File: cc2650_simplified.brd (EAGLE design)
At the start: 50.5 x 22.9 mm, 13 parts, among them IC4 CC2650MODAMOHR, U402 TPS62233DRY

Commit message: Changed Voltage Regulator to 3.3V output.
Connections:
- removed net NRESET: IC4.13, JP2.16, JTAG_CONNECTOR.10
- removed net VBAT: JP3.3
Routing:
- net NRESET: track 41.6 -> 0.00 mm
- net VBAT: track 19.8 -> 0.00 mm
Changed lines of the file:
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@@
 <wire x1="13.08" y1="1.4" x2="15.62" y2="1.4" width="0" layer="19" extent="1-1"/>
-</signal>
-<signal name="NRESET">
-<contactref element="JTAG_CONNECTOR" pad="10"/>
-<contactref element="IC4" pad="13"/>
-<contactref element="JP2" pad="16"/>
-<wire x1="33.5" y1="9.5" x2="34" y2="9.5" width="0.2032" layer="1"/>
-<wire x1="30" y1="6" x2="33.5" y2="9.5" width="0.2032" layer="1"/>
-<wire x1="30" y1="5" x2="30" y2="6" width="0.2032" layer="1"/>
-<wire x1="34" y1="9.5" x2="33.83" y2="9.6" width="0.2032" layer="1"/>
-<wire x1="26.5" y1="3" x2="27.5" y2="4" width="0.2032" layer="1"/>
-<wire x1="27.5" y1="4" x2="27.682" y2="4.27" width="0.2032" layer="1"/>
-<wire x1="5.46" y1="1.4" x2="5.46" y2="1.46" width="0.2" layer="16"/>
-<wire x1="5.46" y1="1.46" x2="7" y2="3" width="0.2" layer="16"/>
-<wire x1="5.46" y1="1.4" x2="5.46" y2="1.46" width="0.2" layer="1"/>
-<wire x1="5.46" y1="1.46" x2="7" y2="3" width="0.2" layer="1"/>
-<wire x1="9" y1="3" x2="7" y2="3" width="0.2" layer="1"/>
-<wire x1="9" y1="3" x2="13.75" y2="3" width="0.2" layer="1"/>
-<wire x1="13.75" y1="3" x2="26.5" y2="3" width="0.2" layer="1"/>
-<wire x1="11.25" y1="5.25" x2="9" y2="3" width="0.2" layer="1"/>
-<wire x1="14.875" y1="4.125" x2="13.75" y2="3" width="0.2" layer="1"/>
-<wire x1="27.682" y1="4.27" x2="29.27" y2="4.27" width="0.2" layer="1"/>
-<wire x1="29.27" y1="4.27" x2="30" y2="5" width="0.2" layer="1"/>
-<wire x1="14.875" y1="4.125" x2="14.875" y2="5.995" width="0.2" layer="1"/>
-<wire x1="14.875" y1="5.995" x2="14.88" y2="6" width="0.2" layer="1"/>
 </signal>
 <signal name="JTAG_TMS">
@@
 <contactref element="IC4" pad="22"/>
 <contactref element="IC4" pad="23"/>
-<contactref element="JTAG_CONNECTOR" pad="1"/>
 <contactref element="JP3" pad="4"/>
 <contactref element="JP3" pad="6"/>
@@
 <wire x1="22.5" y1="9" x2="23.5" y2="9" width="0.2032" layer="1"/>
 <wire x1="22.5" y1="9" x2="22" y2="9" width="0.2032" layer="1"/>
-<wire x1="23.5" y1="9" x2="23.618" y2="9.35" width="0.2032" layer="1"/>
 <wire x1="41.5" y1="4.5" x2="41" y2="4.5" width="0.2032" layer="1"/>
 <wire x1="41" y1="4.5" x2="40.68" y2="4.55" width="0.2032" layer="1"/>
@@
 <wire x1="12.87825625" y1="2.9906" x2="14.9906" y2="2.9906" width="0.2" layer="16"/>
 <via x="17" y="4.5" extent="1-16" drill="0.35"/>
+<contactref element="JTAG_CONNECTOR" pad="1"/>
+<wire x1="23.5" y1="9" x2="23.618" y2="9.35" width="0" layer="19" extent="1-1"/>
 <wire x1="17.75" y1="5.25" x2="20.35" y2="7.35" width="0" layer="19" extent="1-1"/>
 </signal>
-<signal name="VBAT">
-<contactref element="JP3" pad="3"/>
-<wire x1="20.5" y1="21.5" x2="15.5" y2="16.5" width="0.2032" layer="16"/>
-<wire x1="20.5" y1="21.5" x2="20.79" y2="21.68" width="0.2032" layer="16"/>
-<wire x1="15.5" y1="16.5" x2="3.146" y2="16.5" width="0.2" layer="16"/>
-</signal>
 <signal name="EN">

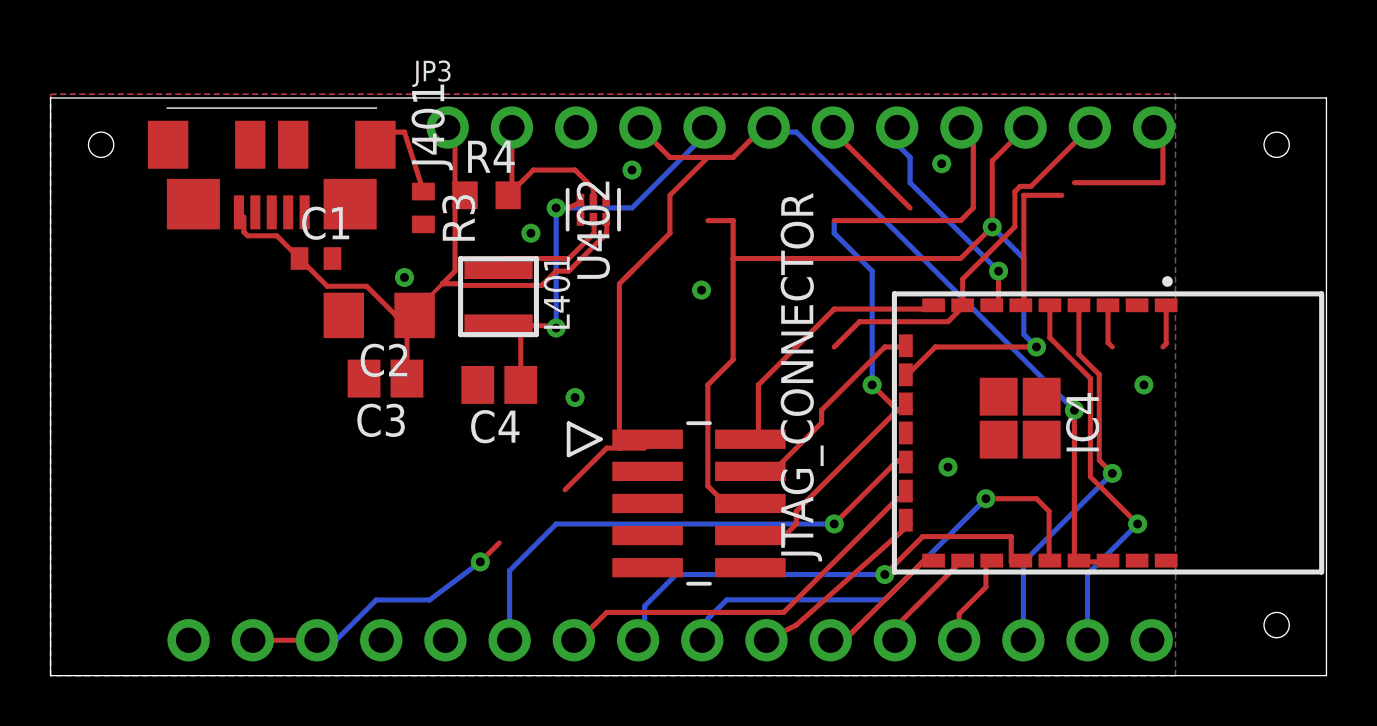
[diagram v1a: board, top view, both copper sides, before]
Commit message: fixed broken connection and missing via.
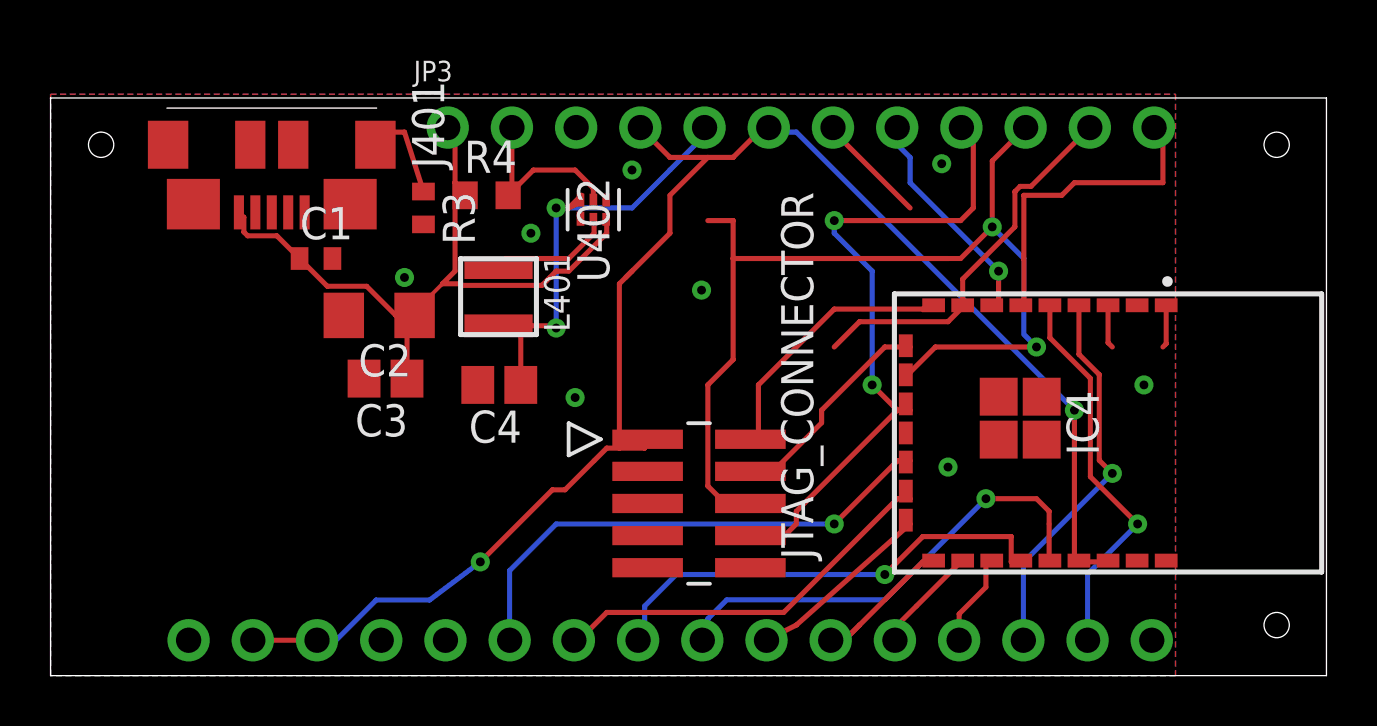
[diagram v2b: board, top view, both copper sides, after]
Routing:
- net VCC: track 58.5 -> 62.3 mm
- net EZFET_VCC: track 19.0 -> 19.9 mm
- net DIO2: track 12.1 -> 12.8 mm
- net DIO6_TDI: vias 1 -> 2
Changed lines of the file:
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@@
 <via x="35.5" y="8.25" extent="1-16" drill="0.35"/>
 <via x="23" y="20" extent="1-16" drill="0.35"/>
-<wire x1="43.25" y1="11.5" x2="44" y2="13" width="0" layer="19" extent="1-1"/>
-<wire x1="42" y1="13" x2="43.25" y2="11.5" width="0" layer="19" extent="1-1"/>
-<wire x1="39.205" y1="11.035" x2="41.83" y2="13.17" width="0" layer="19" extent="1-1"/>
-<wire x1="37.505" y1="11.035" x2="39.205" y2="11.035" width="0" layer="19" extent="1-1"/>
-<wire x1="39.205" y1="9.335" x2="39.205" y2="11.035" width="0" layer="19" extent="1-1"/>
-<wire x1="37.505" y1="9.335" x2="37.505" y2="11.035" width="0" layer="19" extent="1-1"/>
-<wire x1="35.5" y1="8.25" x2="37.505" y2="9.335" width="0" layer="19" extent="1-1"/>
-<wire x1="44.13" y1="4.55" x2="39.205" y2="9.335" width="0" layer="19" extent="1-1"/>
-<wire x1="43.56" y1="1.4" x2="44.13" y2="4.55" width="0" layer="19" extent="1-1"/>
-<wire x1="35.25" y1="20.25" x2="41.83" y2="14.65" width="0" layer="19" extent="1-1"/>
-<wire x1="25.75" y1="15.25" x2="35.25" y2="20.25" width="0" layer="19" extent="1-1"/>
-<wire x1="21.978" y1="18.811" x2="25.75" y2="15.25" width="0" layer="19" extent="1-1"/>
-<wire x1="20.962" y1="18.0744" x2="21.978" y2="18.811" width="0" layer="19" extent="1-1"/>
-<wire x1="23" y1="20" x2="21.978" y2="18.811" width="0" layer="19" extent="1-1"/>
-<wire x1="19" y1="17.5" x2="20.962" y2="18.0744" width="0" layer="19" extent="1-1"/>
-<wire x1="14.75" y1="17.85" x2="19" y2="17.5" width="0" layer="19" extent="1-1"/>
-<wire x1="14" y1="15.75" x2="14.75" y2="17.85" width="0" layer="19" extent="1-1"/>
-<wire x1="11.6" y1="14.25" x2="14" y2="15.75" width="0" layer="19" extent="1-1"/>
-<wire x1="11.15" y1="16.5" x2="11.6" y2="14.25" width="0" layer="19" extent="1-1"/>
-<wire x1="10.05" y1="18.325" x2="11.15" y2="16.5" width="0" layer="19" extent="1-1"/>
-<wire x1="12.4" y1="11.75" x2="11.6" y2="14.25" width="0" layer="19" extent="1-1"/>
-<wire x1="16.9" y1="11.5" x2="12.4" y2="11.75" width="0" layer="19" extent="1-1"/>
-<wire x1="20.75" y1="11" x2="16.9" y2="11.5" width="0" layer="19" extent="1-1"/>
-<wire x1="23.618" y1="8.08" x2="20.75" y2="11" width="0" layer="19" extent="1-1"/>
-<wire x1="23.618" y1="6.81" x2="23.618" y2="8.08" width="0" layer="19" extent="1-1"/>
-<wire x1="23.618" y1="4.27" x2="23.618" y2="6.81" width="0" layer="19" extent="1-1"/>
-<wire x1="15.62" y1="1.4" x2="23.618" y2="4.27" width="0" layer="19" extent="1-1"/>
-<wire x1="13.08" y1="1.4" x2="15.62" y2="1.4" width="0" layer="19" extent="1-1"/>
 </signal>
 <signal name="JTAG_TMS">
@@
 <wire x1="27.682" y1="5.54" x2="29.04" y2="5.54" width="0.2" layer="1"/>
 <wire x1="29.04" y1="5.54" x2="29.5" y2="6" width="0.2" layer="1"/>
-<wire x1="31" y1="18" x2="31" y2="18" width="0" layer="19" extent="1-16"/>
+<via x="31" y="18" extent="1-16" drill="0.35"/>
 </signal>
 <signal name="DIO7">
@@
 <wire x1="44" y1="21.5" x2="43.65" y2="21.68" width="0.2032" layer="1"/>
 <wire x1="44" y1="19.5" x2="40.5" y2="19.5" width="0.2032" layer="1"/>
-<wire x1="40" y1="19" x2="40.5" y2="19.5" width="0" layer="19" extent="1-1"/>
+<wire x1="40.5" y1="19.5" x2="40" y2="19" width="0.2032" layer="1"/>
 </signal>
 <signal name="DIO3">
@@
 <wire x1="18.6" y1="11.5" x2="18.6" y2="13.44" width="0.2" layer="1"/>
 <wire x1="18.6" y1="13.44" x2="19" y2="13.84" width="0.2" layer="1"/>
-<wire x1="21" y1="18.75" x2="20.962" y2="18.811" width="0" layer="19" extent="1-1"/>
+<wire x1="20.5" y1="18.5" x2="21" y2="19" width="0.2032" layer="1"/>
+<wire x1="21" y1="19" x2="20.962" y2="18.811" width="0.2032" layer="1"/>
 </signal>
 <signal name="DIO14">
@@
 <wire x1="23" y1="16" x2="22.5" y2="15.5" width="0.2" layer="1"/>
 <wire x1="22.5" y1="15.5" x2="22.5" y2="9" width="0.2" layer="1"/>
-<wire x1="20.35" y1="7.35" x2="21.5" y2="8.5" width="0.2" layer="1"/>
+<wire x1="21.5" y1="8.5" x2="20.35" y2="7.35" width="0.2" layer="1"/>
 <wire x1="26" y1="20.5" x2="24.5" y2="19" width="0.2" layer="1"/>
 <wire x1="8" y1="1.4" x2="10.54" y2="1.4" width="0.2" layer="1"/>
-<wire x1="17.75" y1="5.25" x2="17" y2="4.5" width="0.2" layer="1"/>
 <wire x1="10.54" y1="1.4" x2="11.28765625" y2="1.4" width="0.2" layer="16"/>
 <wire x1="14.9906" y1="2.9906" x2="17" y2="4.5" width="0.2" layer="16"/>
@@
 <via x="17" y="4.5" extent="1-16" drill="0.35"/>
 <contactref element="JTAG_CONNECTOR" pad="1"/>
-<wire x1="23.5" y1="9" x2="23.618" y2="9.35" width="0" layer="19" extent="1-1"/>
-<wire x1="17.75" y1="5.25" x2="20.35" y2="7.35" width="0" layer="19" extent="1-1"/>
+<wire x1="20.35" y1="7.35" x2="19.85" y2="7.35" width="0.2" layer="1"/>
+<wire x1="19.85" y1="7.35" x2="17" y2="4.5" width="0.2" layer="1"/>
+<wire x1="23.5" y1="9" x2="23.618" y2="9.35" width="0.2032" layer="1"/>
 </signal>
 <signal name="EN">

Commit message: fixed minor connections.
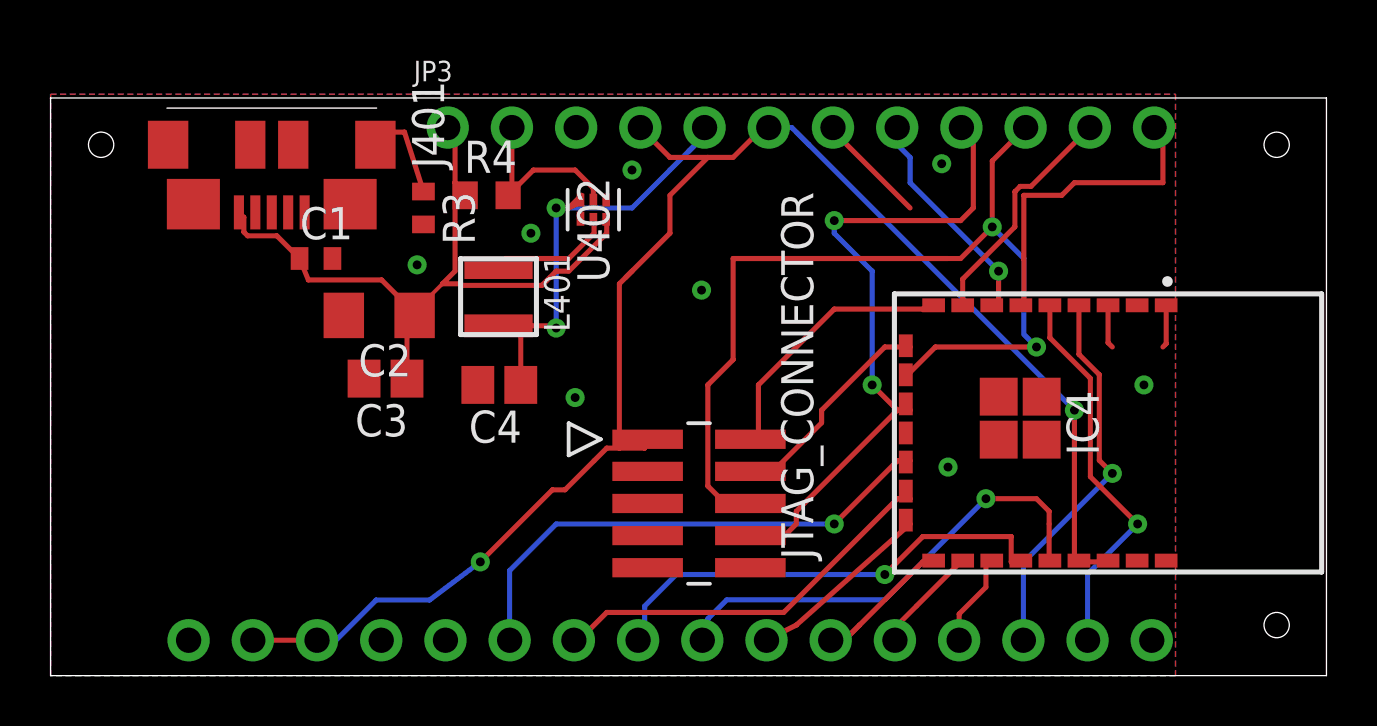
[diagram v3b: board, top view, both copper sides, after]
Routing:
- net DIO4: track 15.2 -> 9.54 mm
- net DIO5_TDO: track 40.6 -> 38.1 mm
- net VCC: track 62.3 -> 63.0 mm
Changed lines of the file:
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@@
 <via x="43.25" y="11.5" extent="1-16" drill="0.35"/>
 <via x="20.75" y="11" extent="1-16" drill="0.35"/>
-<via x="14" y="15.75" extent="1-16" drill="0.35"/>
+<via x="14.5" y="16.25" extent="1-16" drill="0.35"/>
 <via x="25.75" y="15.25" extent="1-16" drill="0.35"/>
 <via x="19" y="17.5" extent="1-16" drill="0.35"/>
@@
 <wire x1="26" y1="11.5" x2="26" y2="7.5" width="0.2032" layer="1"/>
 <wire x1="27" y1="12.5" x2="26" y2="11.5" width="0.2032" layer="1"/>
-<wire x1="27" y1="18" x2="27" y2="16.5" width="0.2032" layer="1"/>
 <wire x1="27" y1="16.5" x2="27" y2="12.5" width="0.2032" layer="1"/>
-<wire x1="26" y1="18" x2="27" y2="18" width="0.2032" layer="1"/>
 <wire x1="27.5" y1="7" x2="27.682" y2="6.81" width="0.2032" layer="1"/>
 <wire x1="27" y1="16.5" x2="35.5" y2="16.5" width="0.2032" layer="1"/>
@@
 <contactref element="IC4" pad="8"/>
 <contactref element="JP3" pad="11"/>
-<wire x1="35.5" y1="14" x2="36" y2="14.5" width="0.2032" layer="1"/>
-<wire x1="32" y1="14" x2="35.5" y2="14" width="0.2032" layer="1"/>
-<wire x1="31" y1="13" x2="32" y2="14" width="0.2032" layer="1"/>
 <wire x1="36" y1="14.5" x2="36.08" y2="14.65" width="0.2032" layer="1"/>
 <wire x1="38.146" y1="19.1466375" x2="38.3533625" y2="19.354" width="0.2" layer="1"/>
@@
 <wire x1="20" y1="18.5" x2="20.5" y2="18.5" width="0.2032" layer="1"/>
 <wire x1="20" y1="18.5" x2="23" y2="18.5" width="0.2032" layer="16"/>
-<wire x1="24.5" y1="20" x2="25.5" y2="21" width="0.2032" layer="16"/>
-<wire x1="25.5" y1="21.5" x2="25.5" y2="21" width="0.2032" layer="16"/>
-<wire x1="25.5" y1="21.5" x2="25.87" y2="21.68" width="0.2032" layer="16"/>
+<wire x1="25.25" y1="20.75" x2="24.5" y2="20" width="0.2032" layer="16"/>
+<wire x1="25.25" y1="20.75" x2="25.5" y2="21" width="0.2032" layer="16"/>
 <wire x1="20" y1="18.5" x2="20" y2="13.75" width="0.2032" layer="16"/>
 <via x="20" y="18.5" extent="1-16" drill="0.35"/>
@@
 <wire x1="20.5" y1="18.5" x2="21" y2="19" width="0.2032" layer="1"/>
 <wire x1="21" y1="19" x2="20.962" y2="18.811" width="0.2032" layer="1"/>
+<wire x1="25.87" y1="21.68" x2="25.87" y2="21.37" width="0.2" layer="16"/>
+<wire x1="25.87" y1="21.37" x2="25.25" y2="20.75" width="0.2" layer="16"/>
 </signal>
 <signal name="DIO14">
@@
 <wire x1="41.5" y1="4.5" x2="41.83" y2="4.55" width="0.2032" layer="1"/>
 <wire x1="40.5" y1="10.5" x2="40.5" y2="4.5" width="0.2032" layer="1"/>
-<wire x1="29.5" y1="21.5" x2="40.5" y2="10.5" width="0.2032" layer="16"/>
-<wire x1="28.5" y1="21.5" x2="29.5" y2="21.5" width="0.2032" layer="16"/>
+<wire x1="30" y1="21" x2="40.5" y2="10.5" width="0.2032" layer="16"/>
+<wire x1="30" y1="21" x2="29.5" y2="21.5" width="0.2032" layer="16"/>
 <wire x1="40.5" y1="4.5" x2="40.68" y2="4.55" width="0.2032" layer="1"/>
-<wire x1="28.5" y1="21.5" x2="28.41" y2="21.68" width="0.2032" layer="16"/>
 <wire x1="24.5" y1="20.5" x2="23.5" y2="21.5" width="0.2032" layer="1"/>
 <wire x1="27" y1="20.5" x2="26" y2="20.5" width="0.2032" layer="1"/>
 <wire x1="26" y1="20.5" x2="24.5" y2="20.5" width="0.2032" layer="1"/>
-<wire x1="28" y1="21.5" x2="27" y2="20.5" width="0.2032" layer="1"/>
 <wire x1="23.5" y1="21.5" x2="23.33" y2="21.68" width="0.2032" layer="1"/>
-<wire x1="28" y1="21.5" x2="28.41" y2="21.68" width="0.2032" layer="1"/>
 <wire x1="22.75" y1="15.75" x2="23" y2="16" width="0.2032" layer="1"/>
 <wire x1="23" y1="16" x2="24.5" y2="17.5" width="0.2032" layer="1"/>
@@
 <wire x1="19.85" y1="7.35" x2="17" y2="4.5" width="0.2" layer="1"/>
 <wire x1="23.5" y1="9" x2="23.618" y2="9.35" width="0.2032" layer="1"/>
+<wire x1="28.41" y1="21.68" x2="29.32" y2="21.68" width="0.2" layer="16"/>
+<wire x1="29.32" y1="21.68" x2="30" y2="21" width="0.2" layer="16"/>
+<wire x1="28.41" y1="21.68" x2="28.18" y2="21.68" width="0.2" layer="1"/>
+<wire x1="28.18" y1="21.68" x2="27" y2="20.5" width="0.2" layer="1"/>
 </signal>
 <signal name="EN">
@@
 <wire x1="14.1" y1="11.75" x2="14.1" y2="13.95" width="0.2" layer="1"/>
 <wire x1="14.1" y1="13.95" x2="14.4" y2="14.25" width="0.2" layer="1"/>
-<wire x1="12.50455" y1="15.4024" x2="10.9476" y2="15.4024" width="0.2" layer="1"/>
-<wire x1="9.85" y1="16.5" x2="10.9476" y2="15.4024" width="0.2" layer="1"/>
+<wire x1="9.85" y1="16.5" x2="10.1976" y2="15.6524" width="0.2" layer="1"/>
 <wire x1="14.25" y1="14.25" x2="14.4" y2="14.25" width="0.2" layer="1"/>
-<wire x1="14.25" y1="14.25" x2="13.65695" y2="14.25" width="0.2" layer="1"/>
-<wire x1="13.65695" y1="14.25" x2="12.50455" y2="15.4024" width="0.2" layer="1"/>
 <wire x1="7.6476" y1="17.54545" x2="7.79545" y2="17.3976" width="0.2" layer="1"/>
 <wire x1="8.9524" y1="17.3976" x2="9.85" y2="16.5" width="0.2" layer="1"/>
-<wire x1="7.45" y1="18.325" x2="7.6476" y2="18.1274" width="0.2" layer="1"/>
+<wire x1="7.6476" y1="18.1274" x2="7.45" y2="18.325" width="0.2" layer="1"/>
 <wire x1="7.6476" y1="18.1274" x2="7.6476" y2="17.54545" width="0.2" layer="1"/>
 <wire x1="7.79545" y1="17.3976" x2="8.9524" y2="17.3976" width="0.2" layer="1"/>
-<wire x1="15.5" y1="15.5" x2="14.25" y2="14.25" width="0.1524" layer="1"/>
+<wire x1="14.375" y1="14.375" x2="15.5" y2="15.5" width="0.1524" layer="1"/>
+<wire x1="14.375" y1="14.375" x2="14.25" y2="14.25" width="0.1524" layer="1"/>
+<wire x1="13.0976" y1="15.6524" x2="14.375" y2="14.375" width="0.2" layer="1"/>
+<wire x1="10.1976" y1="15.6524" x2="13.0976" y2="15.6524" width="0.2" layer="1"/>
 </signal>
 <signal name="N$1">

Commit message: moved headers & usb away from edge of board
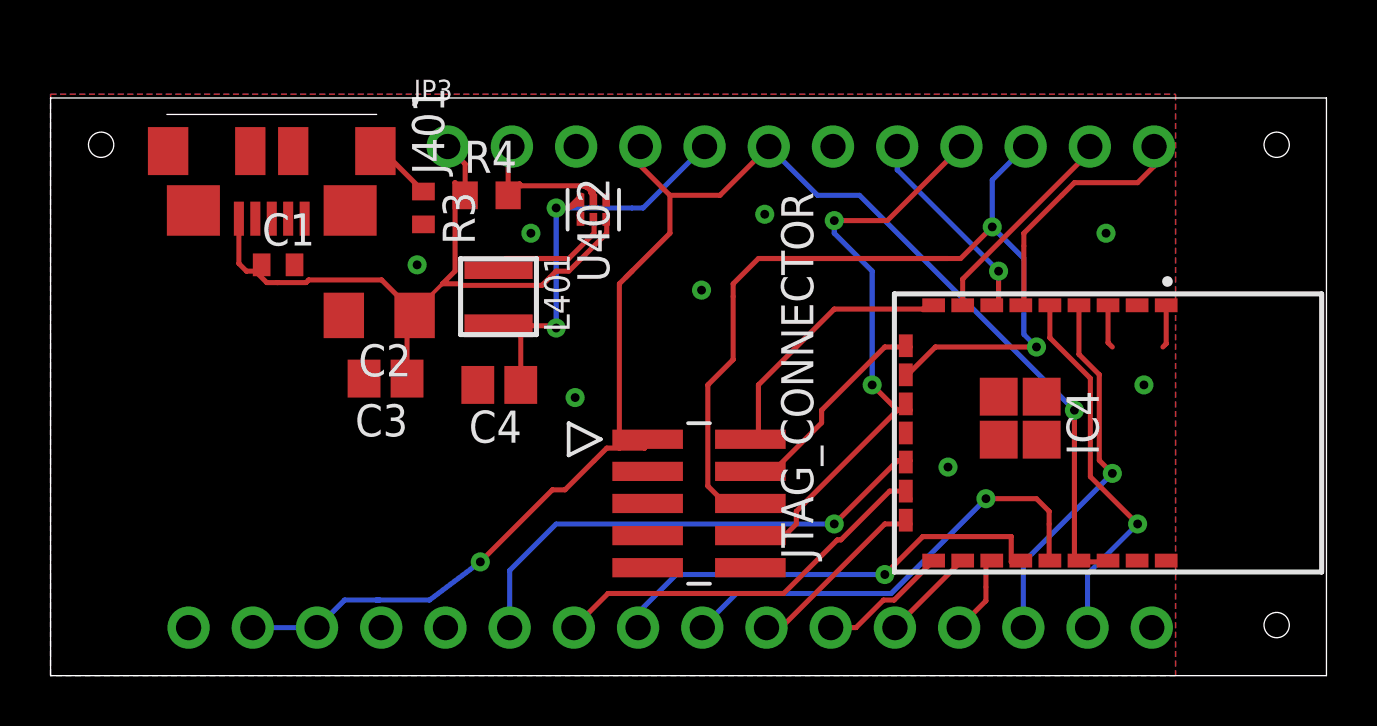
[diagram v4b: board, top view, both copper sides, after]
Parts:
- moved C1 1.52 mm to (9.00, 16.2)
- moved JP3 0.75 mm to (29.7, 20.9)
- moved JP2 0.50 mm to (24.5, 1.90)
- moved J401 0.25 mm to (8.75, 20.8)
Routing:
- net PWR_LED_JMPR: track 4.43 -> 0.00 mm
- net DIO6_TDI: track 26.7 -> 23.7 mm
- net DIO2: track 12.8 -> 10.2 mm
- net VCC: track 63.0 -> 60.9 mm
- net DIO5_TDO: track 38.1 -> 36.4 mm
- net DIO4: track 9.54 -> 8.53 mm
- net DIO10_CLK: track 6.06 -> 5.17 mm
- net EN: track 7.08 -> 6.23 mm
- net EZFET_VCC: track 20.2 -> 19.3 mm
- net DIO3: track 9.15 -> 8.40 mm
- net VBUS: track 28.8 -> 29.5 mm
- net N$1: track 3.99 -> 3.33 mm
- net DIO14: track 18.7 -> 18.1 mm
- net DIO13: track 18.6 -> 18.0 mm
- net DIO7: track 20.6 -> 20.1 mm
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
